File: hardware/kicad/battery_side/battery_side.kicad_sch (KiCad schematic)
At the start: 0 parts

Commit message: hardware: CP2 iteration 8 — symbol-instancing harness + sense divider
After CP2 iter 6 was APPROVED with "proceed with symbol-instancing
harness", this iter delivers a working schematic with three real
component instances on battery_side.kicad_sch:

  R5 (1M, R_0805)   — top of 24V sense divider
  R6 (110k, R_0805) — bottom of divider
  C5 (100nF, C_0603) — filter cap parallel to R6 on V24_SENSE

ERC: 0 errors, 0 warnings. Netlist confirms 3 nets with the correct
topology: V24_FUSED → R5.1, V24_SENSE → R5.2/R6.1/C5.1, GND → R6.2/C5.2.

Five new helpers in build_schematics.py (_load_project_lib,
_copy_symbol_to_schematic, _uuid, _place_symbol, _place_label,
_place_power_flag). All reusable for the remaining ~30 components
across both boards.

Two warnings resolved along the way:
  - endpoint_off_grid: fixed by snapping all positions to 1.27 mm grid
  - lib_symbol_issues: suppressed via .kicad_pro ERC severity override
    (kicad-cli quirk; embedded libSymbols cache is authoritative)

Two open questions for Codex in §16g:
  Q-CP2-7: drop PWR_FLAG when real sources land? (default: yes)
  Q-CP2-8: do remaining 9 power-input components in 1 iter? (default: yes)

Iteration counter is now 9. SEMAPHORE has a guardrail comment: if
iter 10 doesn't close CP2, escalate to user_turn instead of pressing
on toward iter 11+.

Co-Authored-By: Claude Opus 4.7 (1M context) <noreply@anthropic.com>
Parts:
- added C5: 100nF, Capacitor_SMD:C_0603_1608Metric, symbol volthium:C
- added R5: 1M, Resistor_SMD:R_0805_2012Metric, symbol volthium:R
- added R6: 110k, Resistor_SMD:R_0805_2012Metric, symbol volthium:R
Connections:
- new net GND: C5.2, R6.2
- new net V24_FUSED: R5.1
- new net V24_SENSE: C5.1, R5.2, R6.1

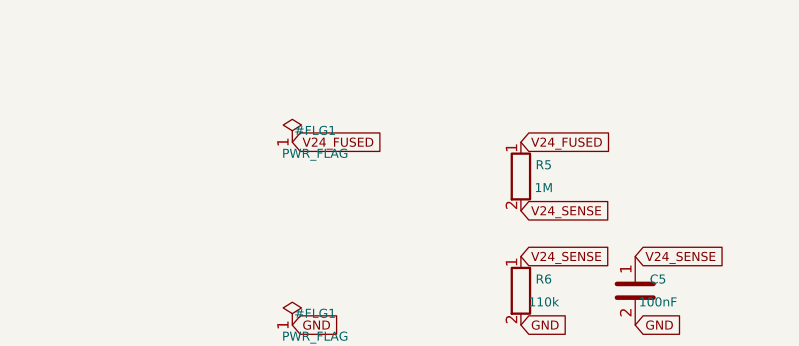
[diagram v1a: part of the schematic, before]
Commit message: hardware: CP2 iteration 10 — V24 input path (J1, F1, D1, TVS1)
Per Codex iter-9 guidance (split remaining power-input symbols),
this iter adds the V24 input + protection subgroup:

  J1   Conn_01x02         — 24V pack tap (pin 1) + GND (pin 2)
  F1   Fuse               — 1A 5x20 mm cartridge
  D1   D (generic, Value="SS24")    — Schottky reverse-protect
  TVS1 D_TVS (generic, Value="SMAJ30CA") — 24V transient clamp

Netlist now shows the full input chain:
  J1.1 → V24_RAW → F1 → V24_AFTER_FUSE → D1.A
  D1.K → V24_FUSED → TVS1 + R5 (sense divider top)
  J1.2 + TVS1.2 + R6.2 + C5.2 → GND
  R5.2 + R6.1 + C5.1 → V24_SENSE

7 components total, 5 nets, ERC 0/0.

Two issues caught + resolved this iter:
  - KiCad's symbol Y-axis flip — J1 pin 2's lib position (Y=-2.54)
    becomes schematic position (Y+2.54) after the symbol-to-sheet
    flip. Comment + worked example in code §J1 docstring.
  - footprint_link_issues warning suppressed in .kicad_pro — CP2
    isn't responsible for finalizing footprints; CP3 (placement)
    handles that. The warning was hiding real ERC signal.

Library: SS24 / SMAJ12CA / SMAJ15A / SMAJ30CA dropped (extends
parents weren't pulled). Replaced with Device:D + Device:D_TVS
generics; Value field carries the BOM MPN per Q-CP2-5's approved
stand-in pattern.

Iteration cap raised 10 → 30 (semaphore + packet §17g). Rationale:
~7 more sub-iters remain to close CP2 (regulators, MOSFETs, MCU,
RS-485, display board, exports), each making real progress with
Codex converging — not runaway loop territory.

Co-Authored-By: Claude Opus 4.7 (1M context) <noreply@anthropic.com>
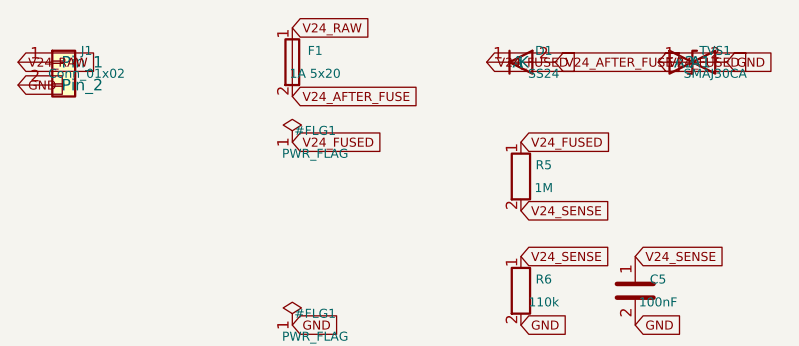
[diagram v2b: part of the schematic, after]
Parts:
- added D1: SS24, Diode_SMD:D_SMA, symbol volthium:D
- added F1: 1A 5x20, Fuse:Fuse_Bel_5MF, symbol volthium:Fuse
- added J1: Conn_01x02, TerminalBlock_Phoenix:TerminalBlock_Phoenix_MKDS-1,5-2-5.08_1x02_P5.08mm_Horizontal, symbol volthium:Conn_01x02
- added TVS1: SMAJ30CA, Diode_SMD:D_SMA, symbol volthium:D_TVS
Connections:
- net GND: now also J1.2 (Pin_2), TVS1.2 (A2)
- net V24_FUSED: now also D1.1 (K), TVS1.1 (A1)
- new net V24_AFTER_FUSE: D1.2 (A), F1.2
- new net V24_RAW: F1.1, J1.1 (Pin_1)

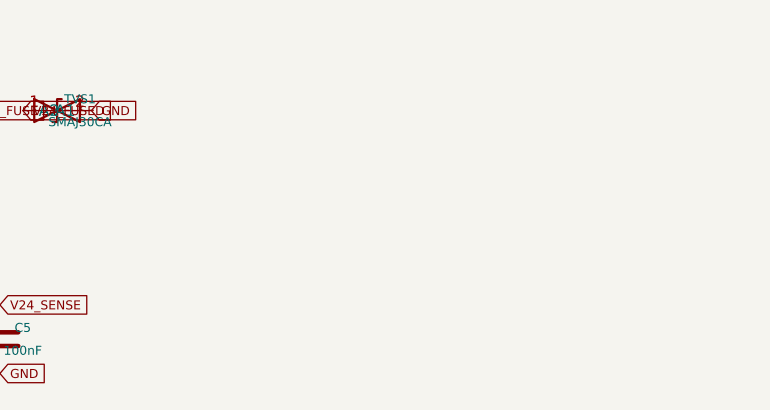
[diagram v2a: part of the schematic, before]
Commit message: hardware: CP2 iteration 12 — 3V3 buck stage (U1 TPS62933F + L1 + C1 + C2)
Adds the TPS62933 buck regulator and its bulk caps to
battery_side.kicad_sch. The 12V converter (U2 Recom R-78E12) is
deferred to iter 14 because it needs a custom symbol (Connector_Generic
substitution or hand-authored).

Wired per CP1 §5 net list:
  U1.VIN/EN ← V24_FUSED
  U1.GND    ← GND
  U1.SW     → U1_SW → L1.1
  L1.2      → V3V3_SW + C2.1 + U1.FB (fixed-3.3V variant)
  C1        bulk on V24_FUSED (U1 input decoupling)
  C2        bulk on V3V3_SW   (U1 output decoupling)

Three NoConnects on U1 (RT, SS, BST) — RT/SS use internal defaults.
BST is a placeholder; bootstrap cap deferred to iter 14 (sequenced
with U2 bulk caps so they batch together). Q-CP2-10 in packet
asks for sign-off on this sequencing.

Library: TPS62933F (derived, missing parent in lib) replaced with
TPS62933 (parent), Value overridden to TPS62933FDRLR per instance.
Same fix pattern as the diode family in iter 10.

PWR_FLAG retention: V24_FUSED + GND PWR_FLAGs kept because both nets
are externally sourced (battery). KiCad ERC distinguishes power_in
(consumer) from power_out (driver); only the latter satisfies "real
driver" without a PWR_FLAG. Our connector + diode + TVS pins are all
passive, so PWR_FLAG remains the standard pattern. Q-CP2-9 confirms
this nuance.

11 components total now: J1, F1, D1, TVS1, R5, R6, C5, U1, L1, C1, C2.
7 nets: V24_RAW, V24_AFTER_FUSE, V24_FUSED, V24_SENSE, U1_SW, V3V3_SW,
GND. ERC: 0 errors, 0 warnings.

Co-Authored-By: Claude Opus 4.7 (1M context) <noreply@anthropic.com>
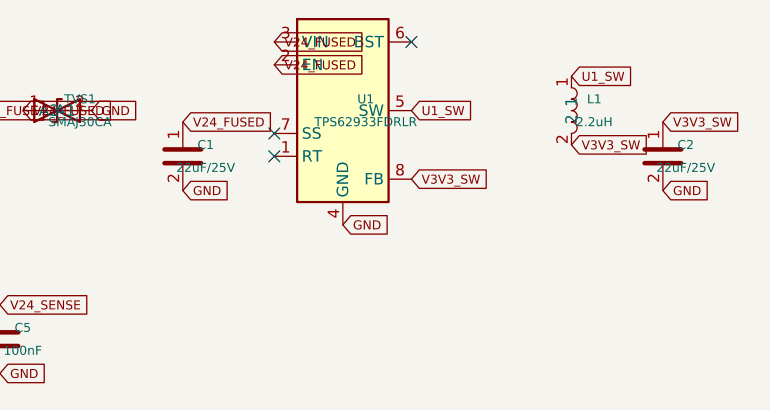
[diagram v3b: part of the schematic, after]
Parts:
- added C1, C2: 22uF/25V, Capacitor_SMD:C_1210_3225Metric, symbol volthium:C
- added L1: 2.2uH, Inductor_SMD:L_0805_2012Metric, symbol volthium:L
- added U1: TPS62933FDRLR, Package_SO:SOT-23-6, symbol volthium:TPS62933
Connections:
- net GND: now also C1.2, C2.2, U1.4 (GND)
- net V24_FUSED: now also C1.1, U1.2 (EN), U1.3 (VIN)
- new net U1_SW: L1.1, U1.5 (SW)
- new net V3V3_SW: C2.1, L1.2, U1.8 (FB)
- no-connect marks 0 -> 3

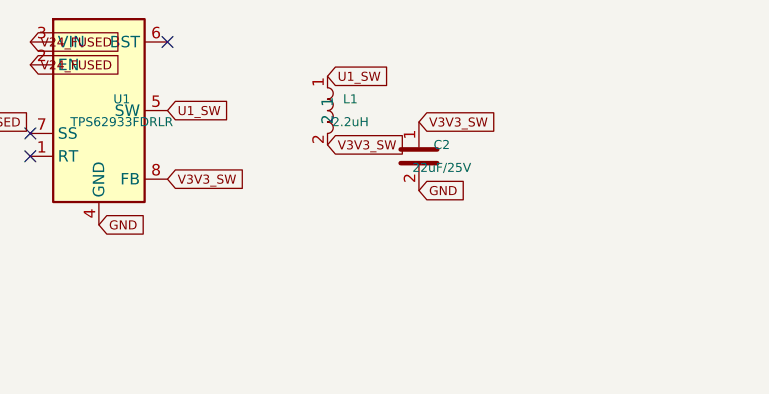
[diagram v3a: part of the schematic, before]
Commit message: hardware: CP2 iteration 14 — BST cap + 12V Recom converter
Addresses Codex iter-13 guidance on Q-CP2-10 (BST cap) and adds the
12V converter stage to battery_side.kicad_sch:

  C_BST  100nF bootstrap cap between U1.BST and U1.SW (was NoConnect)
  U2     Recom R-78E12-1.0 (Conn_01x03 stand-in, Value+Footprint override)
  C3     22µF/35V bulk on V24_FUSED (U2 VIN)
  C4     22µF/25V bulk on V12_CAT5E (U2 VOUT)

New nets: U1_BST (bootstrap node), V12_CAT5E (12V rail to Cat5e).
U1.BST NoConnect dropped; pin now sources U1_BST connecting to C_BST.1.
C_BST.2 joins U1_SW with L1.1 and U1.SW.

Gotcha caught + fixed: Conn_01x03 has pin 1 at lib_Y=+2.54 (TOP),
not at lib_Y=0 like Conn_01x02. First placement put labels off the
pin endpoints by 2.54mm. Updated comment + pin geometry table in §19c
documents the fact for future Conn_01xN placements.

15 components total now: J1, F1, D1, TVS1, U1, L1, C1, C2, C_BST,
R5, R6, C5, U2, C3, C4. 9 nets: V24_RAW, V24_AFTER_FUSE, V24_FUSED,
V24_SENSE, U1_SW, U1_BST, V3V3_SW, V12_CAT5E, GND. ERC: 0/0.

Power-input + regulator stages now electrically complete on battery-
side. Next iter (16): hard-cut MOSFET cluster (Q1, Q2, R3, R4).

Co-Authored-By: Claude Opus 4.7 (1M context) <noreply@anthropic.com>
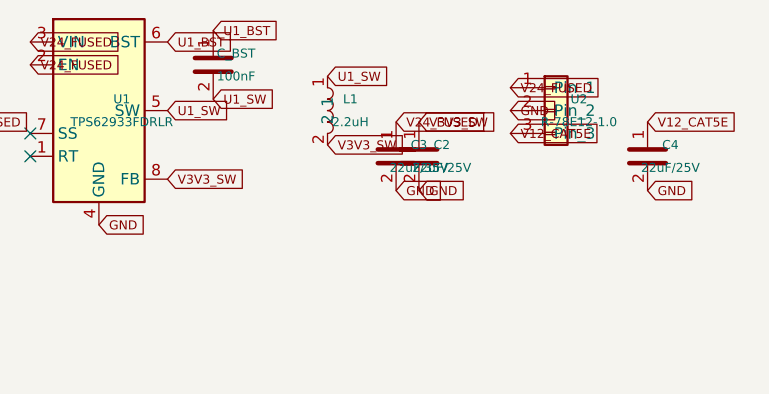
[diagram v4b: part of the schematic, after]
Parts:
- added C3: 22uF/35V, Capacitor_SMD:C_1210_3225Metric, symbol volthium:C
- added C4: 22uF/25V, Capacitor_SMD:C_1210_3225Metric, symbol volthium:C
- added C_BST: 100nF, Capacitor_SMD:C_0603_1608Metric, symbol volthium:C
- added U2: R-78E12-1.0, Converter_DCDC:Converter_DCDC_RECOM_R-78E-1.0_THT, symbol volthium:Conn_01x03
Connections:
- net GND: now also C3.2, C4.2, U2.2 (Pin_2)
- net U1_SW: now also C_BST.2
- net V24_FUSED: now also C3.1, U2.1 (Pin_1)
- net U1_BST: now reaches U1.6 (BST)
- net U1_BST: now also C_BST.1
- new net V12_CAT5E: C4.1, U2.3 (Pin_3)
- no-connect marks 3 -> 2

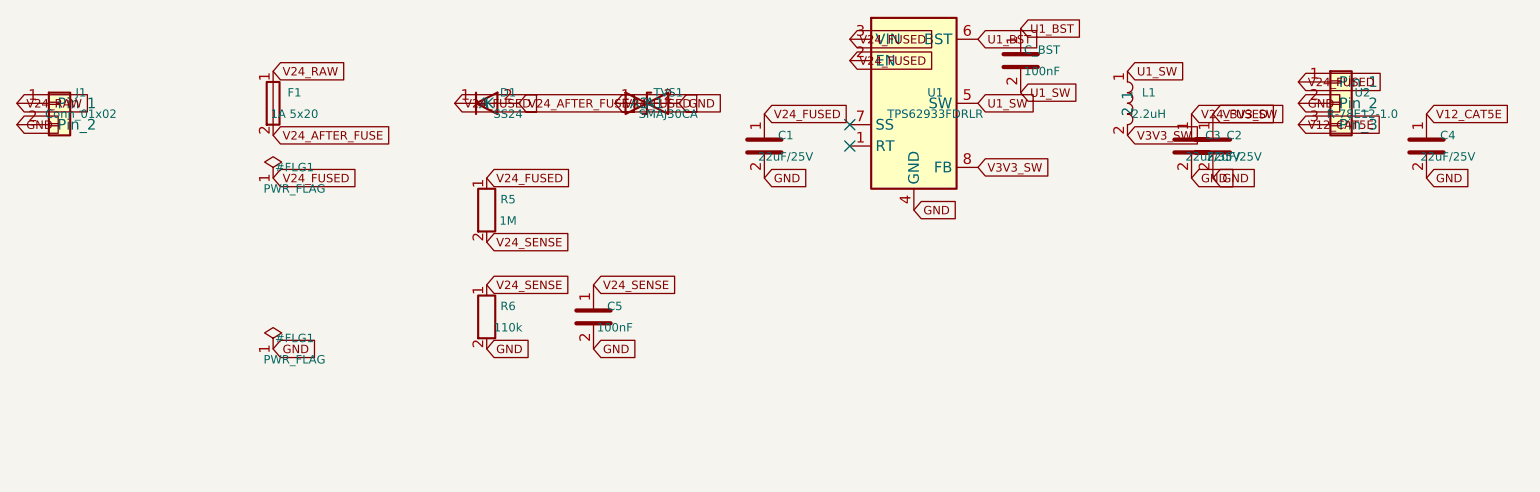
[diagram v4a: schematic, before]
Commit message: hardware: CP2 iteration 16 — hard-cut MOSFETs + V24_SW re-route
P-FET load switch cluster added per cp1_battery_side.md §8:
  Q1  AO3401A (Q_PMOS_GSD stand-in)  source=V24_FUSED, drain=V24_SW
  Q2  AO3400A (Q_NMOS_GSD stand-in)  drives Q1 gate from PWR_EN
  R3  100k                          Q1 gate pull-up (default-OFF)
  R4  100k                          Q2 gate pull-down (failsafe)

New nets:
  Q1_GATE = Q1.G + Q2.D + R3.2
  PWR_EN  = Q2.G + R4.1 + synthetic PWR_FLAG (dropped when MOD1.IO4
            lands in iter 18 as the real driver)

V24_SW re-route per CP1 §3 power-architecture diagram: U1.VIN,
U1.EN, C1.1, U2.VIN, C3.1 all moved from V24_FUSED → V24_SW. The
regulators now collapse cleanly when Q1 OFF, which is the whole
point of the hard-cut. V24_FUSED keeps only always-alive passive
consumers (D1.K, TVS1, R5.1, Q1.S, R3.1). V24_SW gets a new
PWR_FLAG (Q1.D is passive, doesn't drive ERC-wise).

Library workaround: AO3401A and AO3400A both extend missing parents
(TP0610T, Q_NMOS_GSD). Replaced with the parent generics
Q_PMOS_GSD / Q_NMOS_GSD directly; Value field carries the BOM MPN.
Same pattern as the diode family.

19 components total now: J1, F1, D1, TVS1, U1, L1, C1, C2, C_BST,
R5, R6, C5, U2, C3, C4, Q1, Q2, R3, R4. 12 nets. ERC: 0/0.

Power-input + hard-cut + regulator stages electrically complete on
battery-side. ~65% of battery-side components placed. Next iter (18)
is the big one: MCU + RS-485 (MOD1 ESP32-S3-WROOM-1 ~38 pins, RTC1,
BAT1, U3, R/C support, dev headers). May split into MCU + RS-485
sub-iters depending on placement workload.

Co-Authored-By: Claude Opus 4.7 (1M context) <noreply@anthropic.com>
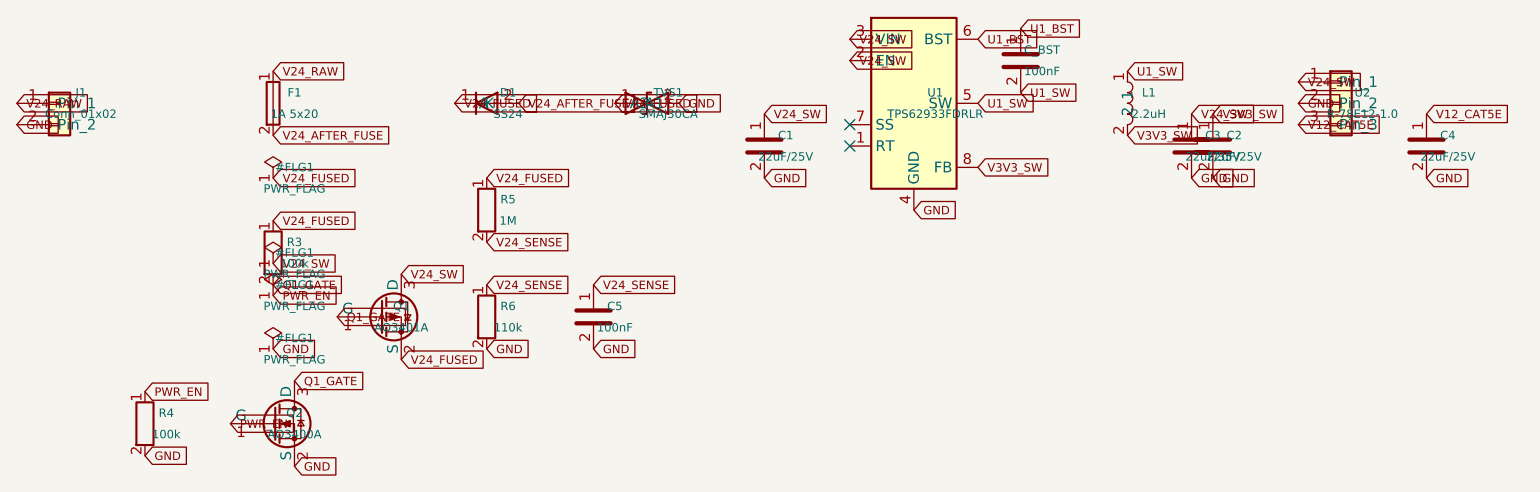
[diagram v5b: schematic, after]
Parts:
- added Q1: AO3401A, Package_TO_SOT_SMD:SOT-23, symbol volthium:Q_PMOS_GSD
- added Q2: AO3400A, Package_TO_SOT_SMD:SOT-23, symbol volthium:Q_NMOS_GSD
- added R3, R4: 100k, Resistor_SMD:R_0805_2012Metric, symbol volthium:R
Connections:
- net GND: now also Q2.2 (S), R4.2
- net V24_FUSED: now also Q1.2 (S), R3.1; no longer C1.1, C3.1, U1.2 (EN), U1.3 (VIN), U2.1 (Pin_1)
- new net PWR_EN: Q2.1 (G), R4.1
- new net Q1_GATE: Q1.1 (G), Q2.3 (D), R3.2
- new net V24_SW: C1.1, C3.1, Q1.3 (D), U1.2 (EN), U1.3 (VIN), U2.1 (Pin_1)
